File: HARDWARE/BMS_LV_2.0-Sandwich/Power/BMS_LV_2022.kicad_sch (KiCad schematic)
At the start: 11 parts, among them J1 Conn_01x26, J2 AS214-97PN, J4 Battery+, J5 Battery-

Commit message: sync
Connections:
- net CAN+: now also J1.17 (Pin_17); no longer J1.16 (Pin_16)
- net CAN-: now also J1.16 (Pin_16); no longer J1.17 (Pin_17)
- net USB-: now reaches J2.J, R14.1
- net USB+: now reaches J2.K, R13.2
- net USB-DM renamed USB1-
- net USB-DP renamed USB1+
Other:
- moved on the sheet: R13, R14

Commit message: Pierwsza wersja bez błędów DRC/ERC, skończony routing plytki control
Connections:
- net VCC is gone; now on net +24V: J1.20 (Pin_20), J2.F
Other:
- moved on the sheet: J1

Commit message: Kolejna kurwa wersja gotowa, japierdole
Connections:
- net Therm_1: no longer names the net of J1.5 (Pin_5)
- net Therm_2: no longer names the net of J1.6 (Pin_6)
- net Therm_3: no longer names the net of J1.7 (Pin_7)
- net Therm_4: no longer names the net of J1.8 (Pin_8)
- net Therm_5: no longer names the net of J1.9 (Pin_9)
- net Therm_6: no longer names the net of J1.10 (Pin_10)
- net Therm_7: no longer names the net of J1.11 (Pin_11)
- net Therm_8: no longer names the net of J1.12 (Pin_12)
- no-connect marks 1 -> 9
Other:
- removed sheet Thermistors

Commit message: V1.0 ready for release
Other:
- note added: "BMS IC"
- note added: "Board to Board"
- note added: "CURRENT SENSOR"
- note added: "FUSES MOSFETS"
- note added: "MISCELLANEOUS"
- moved on the sheet: H1, H2, H3, H4, J1, J2, J4, J5, R13, R14, R15

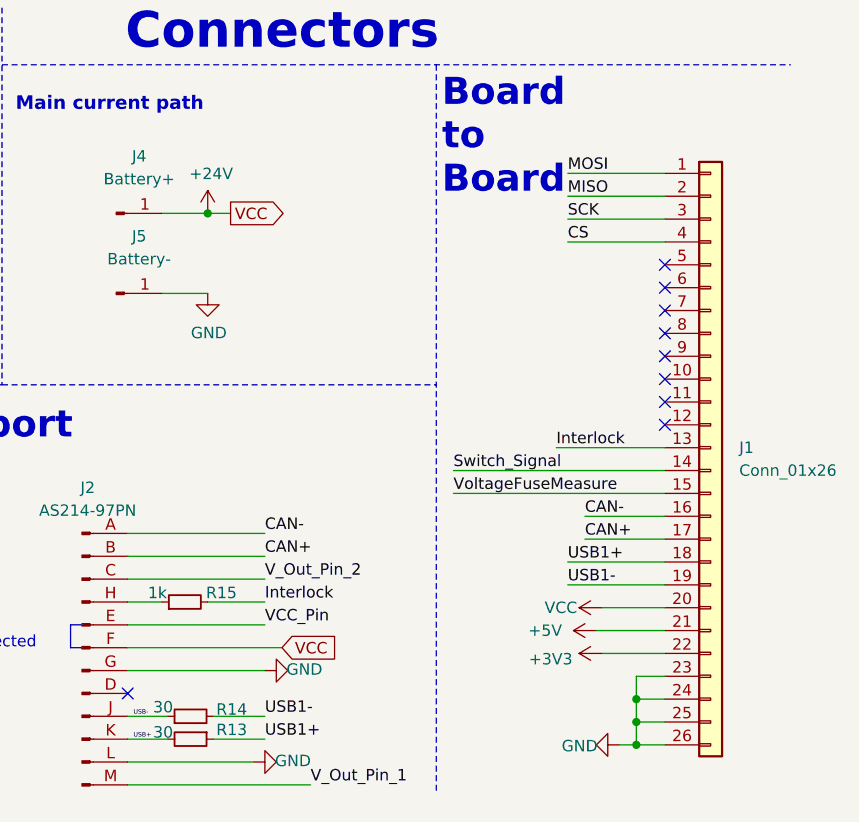
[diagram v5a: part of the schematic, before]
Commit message: Naprawiono: załączanie lv, brak zlącza programatora (XD) oraz brak podłączenia czujnika prądu :9
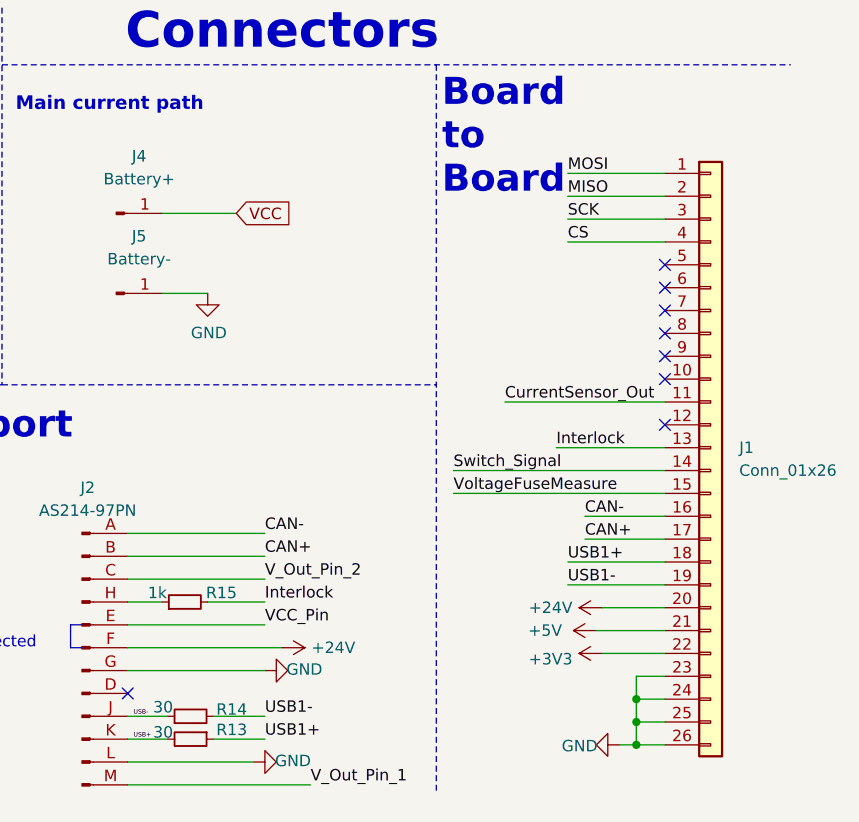
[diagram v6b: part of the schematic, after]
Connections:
- net +24V: no longer J4.1 (Pin_1)
- net CurrentSensor_Out: now also J1.11 (Pin_11)
- new net VCC: J4.1 (Pin_1)
- no-connect marks 9 -> 8
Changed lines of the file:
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@@
-	)
-	(junction
-		(at 129.54 36.195)
-		(diameter 0)
-		(color 0 0 0 0)
 	)
 	(junction
@@
 	)
 	(no_connect
-		(at 180.34 57.15)
-	)
-	(no_connect
 		(at 180.34 44.45)
 	)
@@
 	(wire
 		(pts
+			(xy 162.56 57.15) (xy 180.34 57.15)
+		)
+		(stroke
+			(width 0)
+			(type default)
+		)
+	)
+	(wire
+		(pts
 			(xy 177.165 92.71) (xy 177.165 90.17)
 		)
@@
 	(wire
 		(pts
-			(xy 129.54 36.195) (xy 132.08 36.195)
-		)
-		(stroke
-			(width 0)
-			(type default)
-		)
-	)
-	(wire
-		(pts
 			(xy 177.165 95.25) (xy 180.34 95.25)
 		)
@@
 	(wire
 		(pts
-			(xy 124.46 36.195) (xy 129.54 36.195)
+			(xy 124.46 36.195) (xy 132.715 36.195)
 		)
 		(stroke
@@
 		)
 	)
+	(label "CurrentSensor_Out"
+		(at 162.56 57.15 0)
+		(effects
+			(font
+				(size 1.27 1.27)
+			)
+			(justify left bottom)
+		)
+	)
 	(label "V_Out_Pin_2"
 		(at 46.355 68.58 0)
@@
 	(global_label "VCC"
 		(shape input)
-		(at 137.795 84.455 0)
+		(at 132.715 36.195 0)
 		(fields_autoplaced yes)
 		(effects
@@
 		)
 		(property "Intersheetrefs" "${INTERSHEET_REFS}"
-			(at 143.7546 84.455 0)
-			(hide yes)
-			(show_name no)
-			(do_not_autoplace no)
-			(effects
-				(font
-					(size 1.27 1.27)
-				)
-				(justify left)
-			)
-		)
-	)
-	(global_label "VCC"
-		(shape output)
-		(at 132.08 36.195 0)
-		(fields_autoplaced yes)
-		(effects
-			(font
-				(size 1.27 1.27)
-			)
-			(justify left)
-		)
-		(property "Intersheetrefs" "${INTERSHEET_REFS}"
-			(at 138.0396 36.195 0)
+			(at 138.6746 36.195 0)
 			(hide yes)
 			(show_name no)
@@
 				(path "/fb6504b5-591d-4b10-ab86-0c46f59e8b7d"
 					(reference "R15")
-					(unit 1)
-				)
-			)
-		)
-	)
-	(symbol
-		(lib_id "BMS_LV_2022-rescue:+24V-power")
-		(at 129.54 36.195 0)
-		(unit 1)
-		(body_style 1)
-		(exclude_from_sim no)
-		(in_bom yes)
-		(on_board yes)
-		(in_pos_files yes)
-		(dnp no)
-		(property "Reference" "#PWR0119"
-			(at 129.54 40.005 0)
-			(hide yes)
-			(show_name no)
-			(do_not_autoplace no)
-			(effects
-				(font
-					(size 1.27 1.27)
-				)
-			)
-		)
-		(property "Value" "+24V"
-			(at 129.921 31.8008 0)
-			(show_name no)
-			(do_not_autoplace no)
-			(effects
-				(font
-					(size 1.27 1.27)
-				)
-			)
-		)
-		(property "Footprint" ""
-			(at 129.54 36.195 0)
-			(hide yes)
-			(show_name no)
-			(do_not_autoplace no)
-			(effects
-				(font
-					(size 1.27 1.27)
-				)
-			)
-		)
-		(property "Datasheet" ""
-			(at 129.54 36.195 0)
-			(hide yes)
-			(show_name no)
-			(do_not_autoplace no)
-			(effects
-				(font
-					(size 1.27 1.27)
-				)
-			)
-		)
-		(property "Description" ""
-			(at 129.54 36.195 0)
-			(hide yes)
-			(show_name no)
-			(do_not_autoplace no)
-			(effects
-				(font
-					(size 1.27 1.27)
-				)
-			)
-		)
-		(pin "1"
-		)
-		(instances
-			(project "BMS_LV_2022"
-				(path "/fb6504b5-591d-4b10-ab86-0c46f59e8b7d"
-					(reference "#PWR0119")
 					(unit 1)
 				)
@@
 	)
 	(symbol
+		(lib_id "BMS_LV_2022-rescue:+24V-power")
+		(at 137.795 84.455 270)
+		(mirror x)
+		(unit 1)
+		(body_style 1)
+		(exclude_from_sim no)
+		(in_bom yes)
+		(on_board yes)
+		(in_pos_files yes)
+		(dnp no)
+		(property "Reference" "#PWR0119"
+			(at 133.985 84.455 0)
+			(hide yes)
+			(show_name no)
+			(do_not_autoplace no)
+			(effects
+				(font
+					(size 1.27 1.27)
+				)
+			)
+		)
+		(property "Value" "+24V"
+			(at 143.51 84.455 90)
+			(show_name no)
+			(do_not_autoplace no)
+			(effects
+				(font
+					(size 1.27 1.27)
+				)
+			)
+		)
+		(property "Footprint" ""
+			(at 137.795 84.455 0)
+			(hide yes)
+			(show_name no)
+			(do_not_autoplace no)
+			(effects
+				(font
+					(size 1.27 1.27)
+				)
+			)
+		)
+		(property "Datasheet" ""
+			(at 137.795 84.455 0)
+			(hide yes)
+			(show_name no)
+			(do_not_autoplace no)
+			(effects
+				(font
+					(size 1.27 1.27)
+				)
+			)
+		)
+		(property "Description" ""
+			(at 137.795 84.455 0)
+			(hide yes)
+			(show_name no)
+			(do_not_autoplace no)
+			(effects
+				(font
+					(size 1.27 1.27)
+				)
+			)
+		)
+		(pin "1"
+		)
+		(instances
+			(project "BMS_LV_2022"
+				(path "/fb6504b5-591d-4b10-ab86-0c46f59e8b7d"
+					(reference "#PWR0119")
+					(unit 1)
+				)
+			)
+		)
+	)
+	(symbol
 		(lib_id "BMS_LV_2022-rescue:GNDPWR-power")
 		(at 29.845 128.905 0)
@@
 				(path "/fb6504b5-591d-4b10-ab86-0c46f59e8b7d"
 					(reference "#PWR0123")
+					(unit 1)
+				)
+			)
+		)
+	)
+	(symbol
+		(lib_id "BMS_LV_2022-rescue:+24V-power")
+		(at 173.355 80.01 90)
+		(unit 1)
+		(body_style 1)
+		(exclude_from_sim no)
+		(in_bom yes)
+		(on_board yes)
+		(in_pos_files yes)
+		(dnp no)
+		(property "Reference" "#PWR0124"
+			(at 177.165 80.01 0)
+			(hide yes)
+			(show_name no)
+			(do_not_autoplace no)
+			(effects
+				(font
+					(size 1.27 1.27)
+				)
+			)
+		)
+		(property "Value" "+24V"
+			(at 167.64 80.01 90)
+			(show_name no)
+			(do_not_autoplace no)
+			(effects
+				(font
+					(size 1.27 1.27)
+				)
+			)
+		)
+		(property "Footprint" ""
+			(at 173.355 80.01 0)
+			(hide yes)
+			(show_name no)
+			(do_not_autoplace no)
+			(effects
+				(font
+					(size 1.27 1.27)
+				)
+			)
+		)
+		(property "Datasheet" ""
+			(at 173.355 80.01 0)
+			(hide yes)
+			(show_name no)
+			(do_not_autoplace no)
+			(effects
+				(font
+					(size 1.27 1.27)
+				)
+			)
+		)
+		(property "Description" ""
+			(at 173.355 80.01 0)
+			(hide yes)
+			(show_name no)
+			(do_not_autoplace no)
+			(effects
+				(font
+					(size 1.27 1.27)
+				)
+			)
+		)
+		(pin "1"
+		)
+		(instances
+			(project "BMS_LV_2022"
+				(path "/fb6504b5-591d-4b10-ab86-0c46f59e8b7d"
+					(reference "#PWR0124")
 					(unit 1)
 				)
@@
 					(unit 1)
 				)
-			)
-		)
-	)
-	(symbol
-		(lib_id "BMS_LV_2022-rescue:VCC-power")
-		(at 173.355 80.01 90)
-		(unit 1)
-		(body_style 1)
-		(exclude_from_sim no)
-		(in_bom yes)
-		(on_board yes)
-		(in_pos_files yes)
-		(dnp no)
-		(property "Reference" "#PWR015"
-			(at 177.165 80.01 0)
-			(hide yes)
-			(show_name no)
-			(do_not_autoplace no)
-			(effects
-				(font
-					(size 1.27 1.27)
-				)
-			)
-		)
-		(property "Value" "VCC"
-			(at 168.783 80.01 90)
-			(show_name no)
-			(do_not_autoplace no)
-			(effects
-				(font
-					(size 1.27 1.27)
-				)
-			)
-		)
-		(property "Footprint" ""
-			(at 173.355 80.01 0)
-			(hide yes)
-			(show_name no)
-			(do_not_autoplace no)
-			(effects
-				(font
-					(size 1.27 1.27)
-				)
-			)
-		)
-		(property "Datasheet" ""
-			(at 173.355 80.01 0)
-			(hide yes)
-			(show_name no)
-			(do_not_autoplace no)
-			(effects
-				(font
-					(size 1.27 1.27)
-				)
-			)
-		)
-		(property "Description" ""
-			(at 173.355 80.01 0)
-			(hide yes)
-			(show_name no)
-			(do_not_autoplace no)
-			(effects
-				(font
-					(size 1.27 1.27)
-				)
-			)
-		)
-		(pin "1"
-		)
-		(instances
-			(project "BMS_LV_2022"
-				(path "/fb6504b5-591d-4b10-ab86-0c46f59e8b7d"
-					(reference "#PWR015")
-					(unit 1)
-				)
